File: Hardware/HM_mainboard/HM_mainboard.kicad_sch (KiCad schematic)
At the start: 0 parts

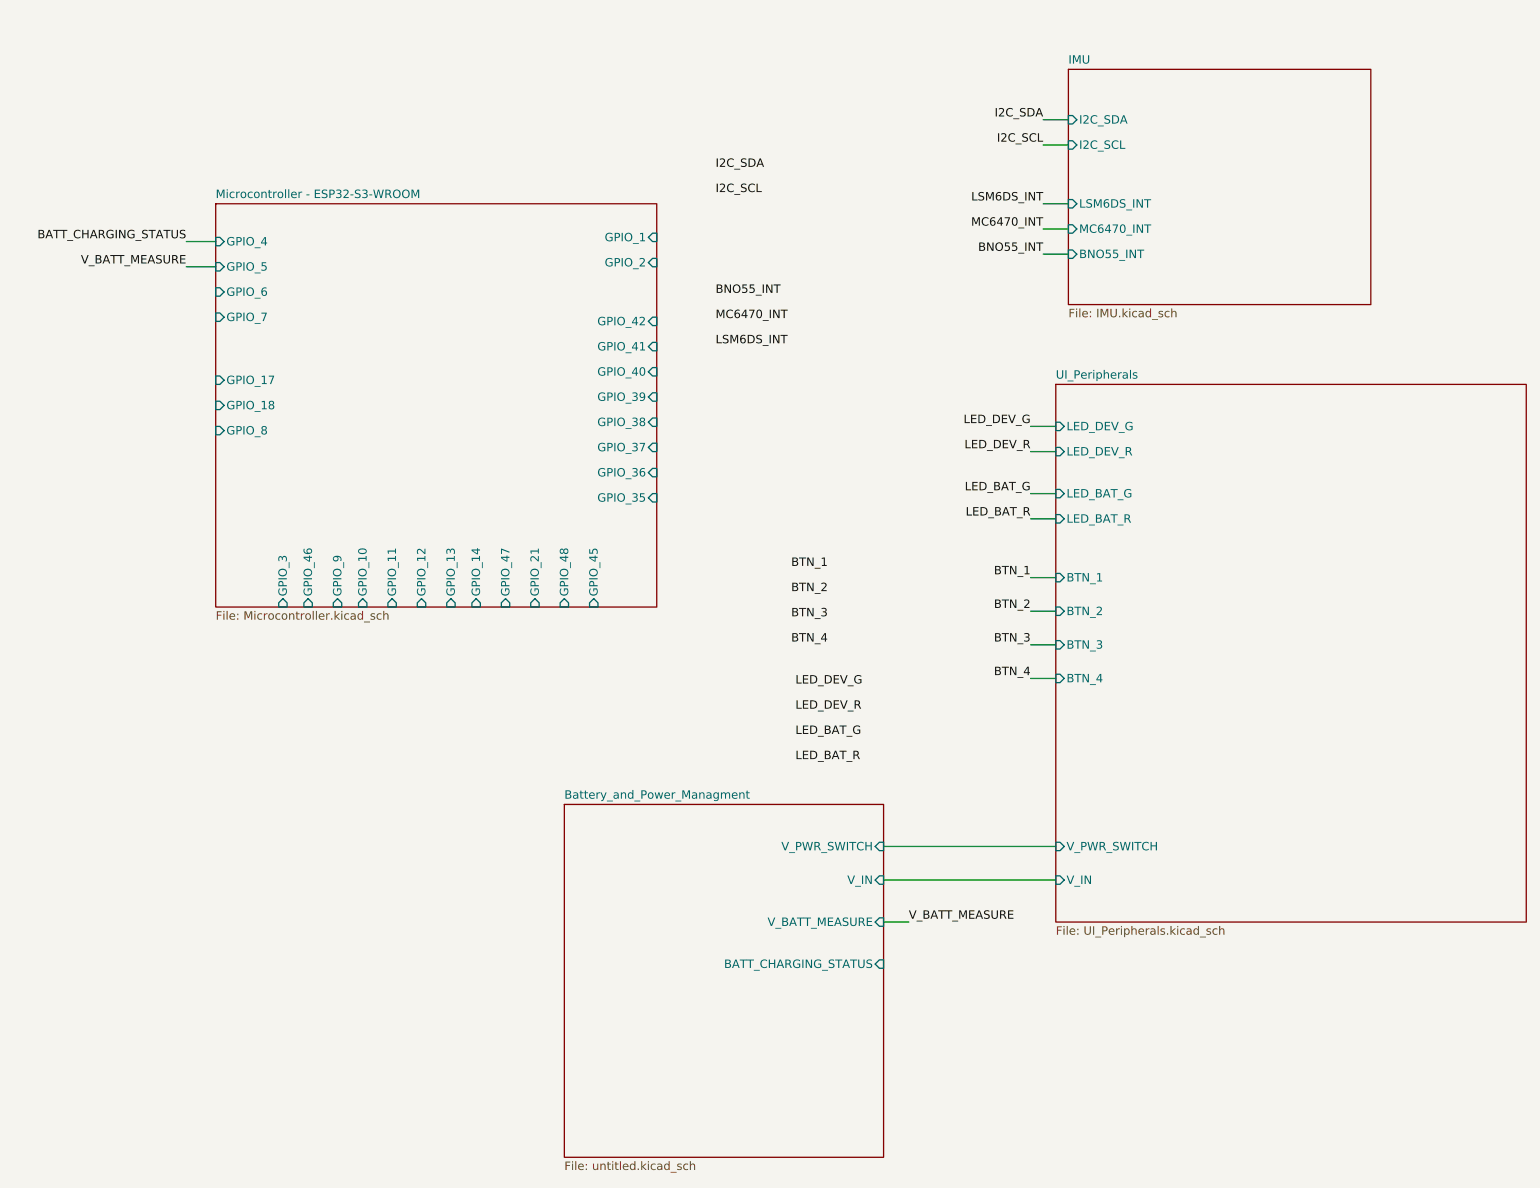
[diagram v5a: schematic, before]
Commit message: Started component placement for PCB
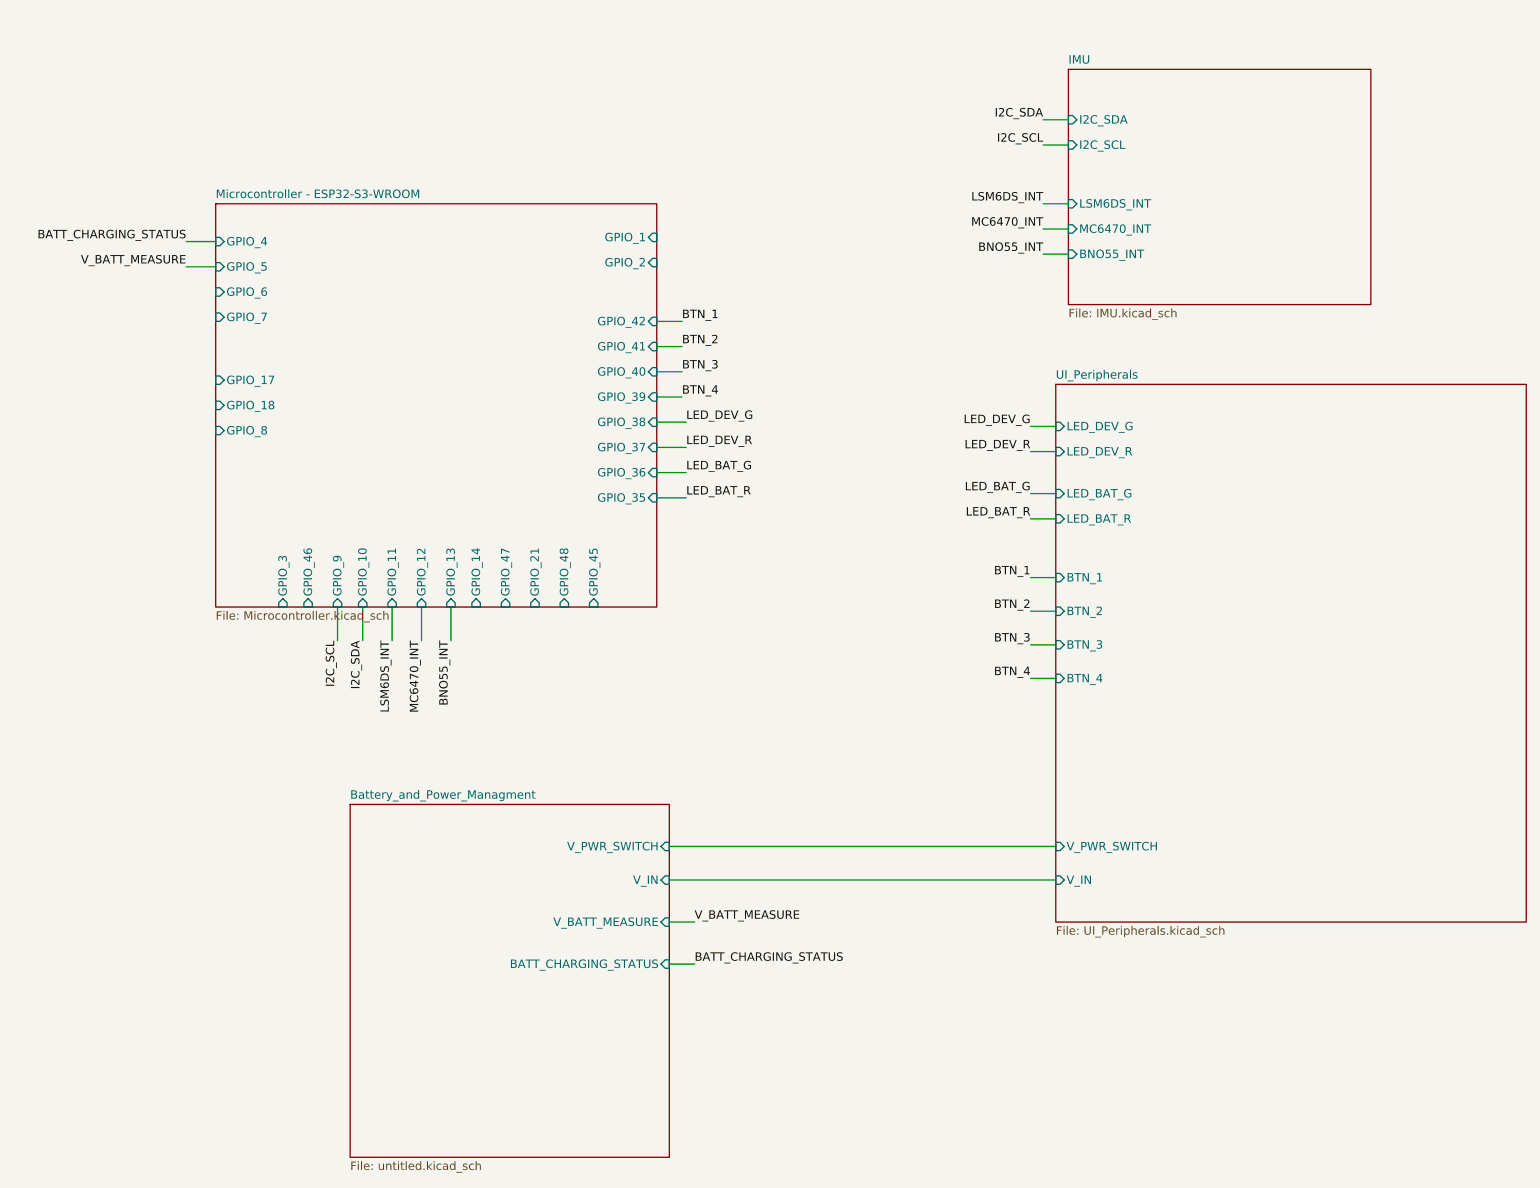
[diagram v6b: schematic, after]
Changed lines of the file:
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@@
+    (stroke (width 0) (type default))
+  )
+  (wire (pts (xy 118.745 157.48) (xy 122.555 157.48))
     (stroke (width 0) (type default))
   )
@@
     (stroke (width 0) (type default))
   )
+  (wire (pts (xy 116.84 79.375) (xy 121.285 79.375))
+    (stroke (width 0) (type default))
+  )
   (wire (pts (xy 173.355 109.22) (xy 177.165 109.22))
     (stroke (width 0) (type default))
   )
+  (wire (pts (xy 116.84 60.325) (xy 120.65 60.325))
+    (stroke (width 0) (type default))
+  )
   (wire (pts (xy 173.355 76.2) (xy 177.165 76.2))
     (stroke (width 0) (type default))
@@
     (stroke (width 0) (type default))
   )
-  (wire (pts (xy 151.13 144.78) (xy 177.165 144.78))
+  (wire (pts (xy 116.84 64.135) (xy 120.65 64.135))
+    (stroke (width 0) (type default))
+  )
+  (wire (pts (xy 76.835 103.505) (xy 76.835 108.585))
+    (stroke (width 0) (type default))
+  )
+  (wire (pts (xy 116.84 83.185) (xy 121.285 83.185))
+    (stroke (width 0) (type default))
+  )
+  (wire (pts (xy 118.745 144.78) (xy 177.165 144.78))
+    (stroke (width 0) (type default))
+  )
+  (wire (pts (xy 72.39 103.505) (xy 72.39 108.585))
     (stroke (width 0) (type default))
   )
@@
     (stroke (width 0) (type default))
   )
+  (wire (pts (xy 81.28 103.505) (xy 81.28 108.585))
+    (stroke (width 0) (type default))
+  )
+  (wire (pts (xy 116.84 71.755) (xy 120.65 71.755))
+    (stroke (width 0) (type default))
+  )
   (wire (pts (xy 173.355 90.17) (xy 177.165 90.17))
     (stroke (width 0) (type default))
@@
     (stroke (width 0) (type default))
   )
+  (wire (pts (xy 85.725 103.505) (xy 85.725 108.585))
+    (stroke (width 0) (type default))
+  )
   (wire (pts (xy 173.355 104.14) (xy 177.165 104.14))
     (stroke (width 0) (type default))
@@
     (stroke (width 0) (type default))
   )
+  (wire (pts (xy 116.84 86.995) (xy 121.285 86.995))
+    (stroke (width 0) (type default))
+  )
   (wire (pts (xy 175.26 46.355) (xy 179.07 46.355))
     (stroke (width 0) (type default))
   )
-  (wire (pts (xy 151.13 139.7) (xy 177.165 139.7))
+  (wire (pts (xy 118.745 139.7) (xy 177.165 139.7))
+    (stroke (width 0) (type default))
+  )
+  (wire (pts (xy 68.58 103.505) (xy 68.58 108.585))
     (stroke (width 0) (type default))
   )
@@
     (stroke (width 0) (type default))
   )
-  (wire (pts (xy 151.13 151.13) (xy 154.94 151.13))
+  (wire (pts (xy 116.84 75.565) (xy 121.285 75.565))
+    (stroke (width 0) (type default))
+  )
+  (wire (pts (xy 118.745 151.13) (xy 122.555 151.13))
+    (stroke (width 0) (type default))
+  )
+  (wire (pts (xy 116.84 67.945) (xy 120.65 67.945))
     (stroke (width 0) (type default))
   )
@@
     (effects (font (size 1.27 1.27)) (justify right bottom))
   )
-  (label "LED_DEV_R" (at 137.795 119.38 0) (fields_autoplaced)
+  (label "LED_DEV_R" (at 121.285 79.375 0) (fields_autoplaced)
     (effects (font (size 1.27 1.27)) (justify left bottom))
   )
@@
     (effects (font (size 1.27 1.27)) (justify right bottom))
   )
-  (label "BTN_3" (at 137.16 105.41 0) (fields_autoplaced)
+  (label "BTN_3" (at 120.65 67.945 0) (fields_autoplaced)
     (effects (font (size 1.27 1.27)) (justify left bottom))
   )
@@
     (effects (font (size 1.27 1.27)) (justify right bottom))
   )
-  (label "I2C_SCL" (at 125.73 41.275 0) (fields_autoplaced)
-    (effects (font (size 1.27 1.27)) (justify left bottom))
-  )
-  (label "BTN_2" (at 137.16 101.6 0) (fields_autoplaced)
+  (label "I2C_SCL" (at 68.58 108.585 270) (fields_autoplaced)
+    (effects (font (size 1.27 1.27)) (justify right bottom))
+  )
+  (label "BTN_2" (at 120.65 64.135 0) (fields_autoplaced)
     (effects (font (size 1.27 1.27)) (justify left bottom))
   )
@@
     (effects (font (size 1.27 1.27)) (justify right bottom))
   )
-  (label "I2C_SDA" (at 125.73 37.465 0) (fields_autoplaced)
-    (effects (font (size 1.27 1.27)) (justify left bottom))
-  )
-  (label "BNO55_INT" (at 125.73 56.515 0) (fields_autoplaced)
-    (effects (font (size 1.27 1.27)) (justify left bottom))
+  (label "I2C_SDA" (at 72.39 108.585 270) (fields_autoplaced)
+    (effects (font (size 1.27 1.27)) (justify right bottom))
+  )
+  (label "BNO55_INT" (at 85.725 108.585 270) (fields_autoplaced)
+    (effects (font (size 1.27 1.27)) (justify right bottom))
   )
   (label "I2C_SDA" (at 175.26 29.845 180) (fields_autoplaced)
@@
     (effects (font (size 1.27 1.27)) (justify right bottom))
   )
-  (label "LED_BAT_G" (at 137.795 123.19 0) (fields_autoplaced)
+  (label "LED_BAT_G" (at 121.285 83.185 0) (fields_autoplaced)
     (effects (font (size 1.27 1.27)) (justify left bottom))
   )
@@
     (effects (font (size 1.27 1.27)) (justify right bottom))
   )
-  (label "BTN_4" (at 137.16 109.22 0) (fields_autoplaced)
+  (label "BTN_4" (at 120.65 71.755 0) (fields_autoplaced)
     (effects (font (size 1.27 1.27)) (justify left bottom))
   )
@@
     (effects (font (size 1.27 1.27)) (justify right bottom))
   )
-  (label "LSM6DS_INT" (at 125.73 64.135 0) (fields_autoplaced)
-    (effects (font (size 1.27 1.27)) (justify left bottom))
+  (label "LSM6DS_INT" (at 76.835 108.585 270) (fields_autoplaced)
+    (effects (font (size 1.27 1.27)) (justify right bottom))
   )
   (label "BNO55_INT" (at 175.26 50.165 180) (fields_autoplaced)
     (effects (font (size 1.27 1.27)) (justify right bottom))
   )
+  (label "BATT_CHARGING_STATUS" (at 122.555 157.48 0) (fields_autoplaced)
+    (effects (font (size 1.27 1.27)) (justify left bottom))
+  )
   (label "I2C_SCL" (at 175.26 33.655 180) (fields_autoplaced)
     (effects (font (size 1.27 1.27)) (justify right bottom))
@@
     (effects (font (size 1.27 1.27)) (justify right bottom))
   )
-  (label "MC6470_INT" (at 125.73 60.325 0) (fields_autoplaced)
-    (effects (font (size 1.27 1.27)) (justify left bottom))
+  (label "MC6470_INT" (at 81.28 108.585 270) (fields_autoplaced)
+    (effects (font (size 1.27 1.27)) (justify right bottom))
   )
   (label "LED_BAT_R" (at 173.355 90.17 180) (fields_autoplaced)
@@
     (effects (font (size 1.27 1.27)) (justify right bottom))
   )
-  (label "BTN_1" (at 137.16 97.79 0) (fields_autoplaced)
-    (effects (font (size 1.27 1.27)) (justify left bottom))
-  )
-  (label "LED_DEV_G" (at 137.795 115.57 0) (fields_autoplaced)
-    (effects (font (size 1.27 1.27)) (justify left bottom))
-  )
-  (label "LED_BAT_R" (at 137.795 127 0) (fields_autoplaced)
-    (effects (font (size 1.27 1.27)) (justify left bottom))
-  )
-  (label "V_BATT_MEASURE" (at 154.94 151.13 0) (fields_autoplaced)
+  (label "BTN_1" (at 120.65 60.325 0) (fields_autoplaced)
+    (effects (font (size 1.27 1.27)) (justify left bottom))
+  )
+  (label "LED_DEV_G" (at 121.285 75.565 0) (fields_autoplaced)
+    (effects (font (size 1.27 1.27)) (justify left bottom))
+  )
+  (label "LED_BAT_R" (at 121.285 86.995 0) (fields_autoplaced)
+    (effects (font (size 1.27 1.27)) (justify left bottom))
+  )
+  (label "V_BATT_MEASURE" (at 122.555 151.13 0) (fields_autoplaced)
     (effects (font (size 1.27 1.27)) (justify left bottom))
   )
@@
     )
   )
-  (sheet (at 102.87 133.35) (size 48.26 53.34) (fields_autoplaced)
+  (sheet (at 70.485 133.35) (size 48.26 53.34) (fields_autoplaced)
     (stroke (width 0.1524) (type solid))
     (fill (color 0 0 0 0.0000))
-    (property "Sheetname" "Battery_and_Power_Managment" (at 102.87 132.6384 0)
+    (property "Sheetname" "Battery_and_Power_Managment" (at 70.485 132.6384 0)
       (effects (font (size 1.27 1.27)) (justify left bottom))
     )
-    (property "Sheetfile" "untitled.kicad_sch" (at 102.87 187.2746 0)
+    (property "Sheetfile" "untitled.kicad_sch" (at 70.485 187.2746 0)
       (effects (font (size 1.27 1.27)) (justify left top))
     )
-    (pin "V_IN" input (at 151.13 144.78 0)
-      (effects (font (size 1.27 1.27)) (justify right))
-    )
-    (pin "V_PWR_SWITCH" input (at 151.13 139.7 0)
-      (effects (font (size 1.27 1.27)) (justify right))
-    )
-    (pin "V_BATT_MEASURE" input (at 151.13 151.13 0)
-      (effects (font (size 1.27 1.27)) (justify right))
-    )
-    (pin "BATT_CHARGING_STATUS" input (at 151.13 157.48 0)
-      (effects (font (size 1.27 1.27)) (justify right))
-    )
+    (pin "V_IN" input (at 118.745 144.78 0)
+      (effects (font (size 1.27 1.27)) (justify right))
+    )
+    (pin "V_PWR_SWITCH" input (at 118.745 139.7 0)
+      (effects (font (size 1.27 1.27)) (justify right))
+    )
+    (pin "V_BATT_MEASURE" input (at 118.745 151.13 0)
+      (effects (font (size 1.27 1.27)) (justify right))
+    )
+    (pin "BATT_CHARGING_STATUS" input (at 118.745 157.48 0)
+      (effects (font (size 1.27 1.27)) (justify right))
+    )

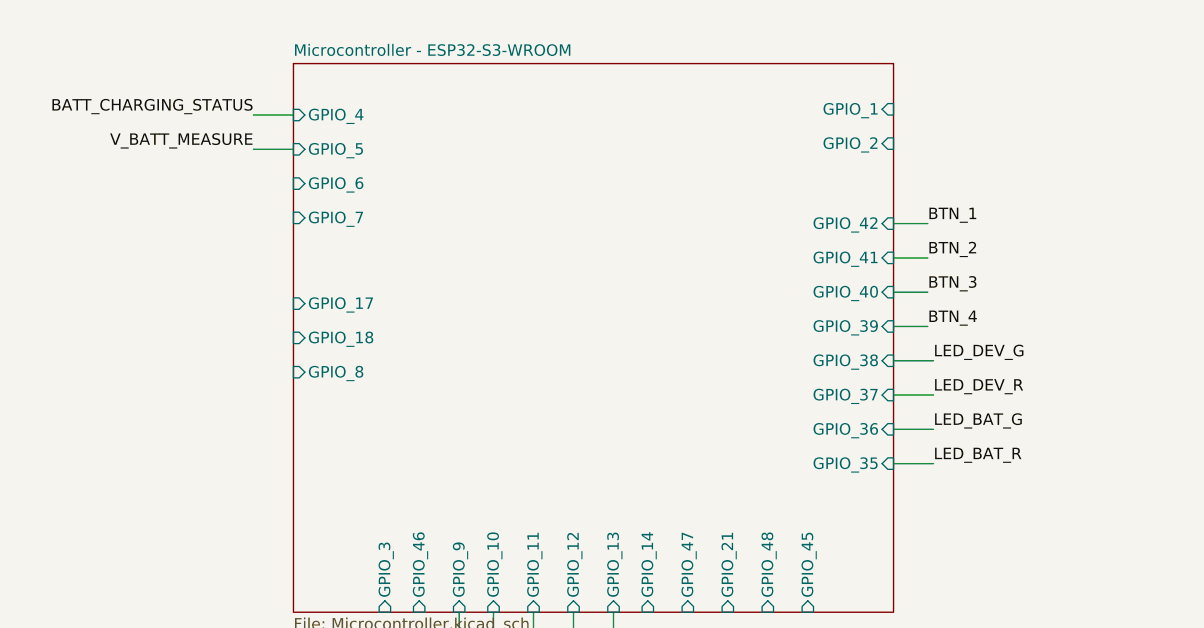
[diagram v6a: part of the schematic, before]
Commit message: Updated footprint of auxiliary jacks, routed first version of PCB
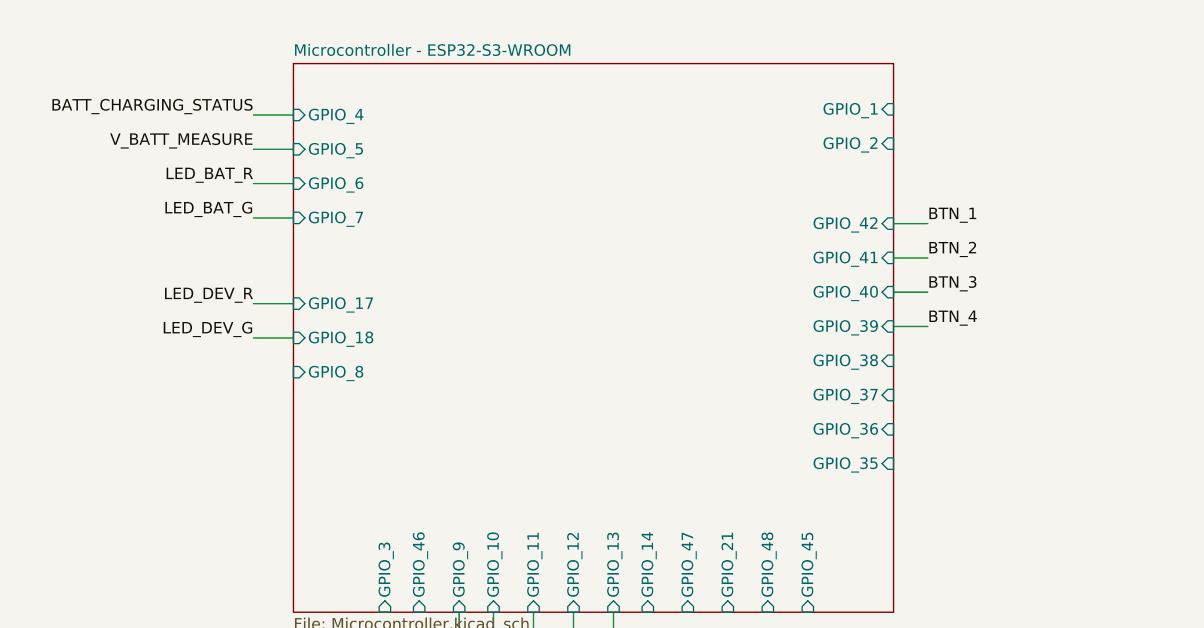
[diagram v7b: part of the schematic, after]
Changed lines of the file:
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@@
-    (stroke (width 0) (type default))
-  )
-  (wire (pts (xy 116.84 79.375) (xy 121.285 79.375))
     (stroke (width 0) (type default))
   )
@@
     (stroke (width 0) (type default))
   )
-  (wire (pts (xy 116.84 83.185) (xy 121.285 83.185))
-    (stroke (width 0) (type default))
-  )
   (wire (pts (xy 118.745 144.78) (xy 177.165 144.78))
     (stroke (width 0) (type default))
@@
     (stroke (width 0) (type default))
   )
-  (wire (pts (xy 116.84 71.755) (xy 120.65 71.755))
+  (wire (pts (xy 45.72 69.215) (xy 50.165 69.215))
     (stroke (width 0) (type default))
   )
   (wire (pts (xy 173.355 90.17) (xy 177.165 90.17))
+    (stroke (width 0) (type default))
+  )
+  (wire (pts (xy 45.72 73.025) (xy 50.165 73.025))
     (stroke (width 0) (type default))
   )
@@
     (stroke (width 0) (type default))
   )
-  (wire (pts (xy 116.84 86.995) (xy 121.285 86.995))
+  (wire (pts (xy 175.26 46.355) (xy 179.07 46.355))
     (stroke (width 0) (type default))
   )
-  (wire (pts (xy 175.26 46.355) (xy 179.07 46.355))
+  (wire (pts (xy 45.72 59.69) (xy 50.165 59.69))
+    (stroke (width 0) (type default))
+  )
+  (wire (pts (xy 45.72 55.88) (xy 50.165 55.88))
     (stroke (width 0) (type default))
   )
@@
     (stroke (width 0) (type default))
   )
-  (wire (pts (xy 116.84 75.565) (xy 121.285 75.565))
+  (wire (pts (xy 118.745 151.13) (xy 122.555 151.13))
     (stroke (width 0) (type default))
   )
-  (wire (pts (xy 118.745 151.13) (xy 122.555 151.13))
+  (wire (pts (xy 116.84 71.755) (xy 120.65 71.755))
     (stroke (width 0) (type default))
   )
@@
     (effects (font (size 1.27 1.27)) (justify right bottom))
   )
-  (label "LED_DEV_R" (at 121.285 79.375 0) (fields_autoplaced)
-    (effects (font (size 1.27 1.27)) (justify left bottom))
+  (label "LED_DEV_R" (at 45.72 69.215 180) (fields_autoplaced)
+    (effects (font (size 1.27 1.27)) (justify right bottom))
   )
   (label "V_BATT_MEASURE" (at 45.72 52.07 180) (fields_autoplaced)
@@
     (effects (font (size 1.27 1.27)) (justify right bottom))
   )
-  (label "LED_BAT_G" (at 121.285 83.185 0) (fields_autoplaced)
-    (effects (font (size 1.27 1.27)) (justify left bottom))
+  (label "LED_BAT_G" (at 45.72 59.69 180) (fields_autoplaced)
+    (effects (font (size 1.27 1.27)) (justify right bottom))
   )
   (label "MC6470_INT" (at 175.26 46.355 180) (fields_autoplaced)
@@
     (effects (font (size 1.27 1.27)) (justify left bottom))
   )
-  (label "LED_DEV_G" (at 121.285 75.565 0) (fields_autoplaced)
-    (effects (font (size 1.27 1.27)) (justify left bottom))
+  (label "LED_DEV_G" (at 45.72 73.025 180) (fields_autoplaced)
+    (effects (font (size 1.27 1.27)) (justify right bottom))
   )
-  (label "LED_BAT_R" (at 121.285 86.995 0) (fields_autoplaced)
-    (effects (font (size 1.27 1.27)) (justify left bottom))
+  (label "LED_BAT_R" (at 45.72 55.88 180) (fields_autoplaced)
+    (effects (font (size 1.27 1.27)) (justify right bottom))
   )
   (label "V_BATT_MEASURE" (at 122.555 151.13 0) (fields_autoplaced)
